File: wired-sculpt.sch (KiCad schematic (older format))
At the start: 26 parts, among them J1 10103594-0001LF, J3 AVR-ISP-6 - NOT FITTED, J4 3-84952-0, SW1 FSMSM, U1 AT90USB1286-AU, U2 USBLC6-2SC6, Y1 TSX-3225 16.0000MF18X-AC6

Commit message: WIP: checkpoint work on rev 3 of the schematic and layout
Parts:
- removed R4, R5, R6: ERJ-3GEYJ331V, Resistor_SMD:R_0603_1608Metric, symbol Device:R_US
- added C10, C11, C12: CL10A105KA8NNNC, Capacitor_SMD:C_0603_1608Metric, symbol Device:C
- added C2: CL21B104KACNNNC, Capacitor_SMD:C_0805_2012Metric, symbol Device:C
- added C3: CL21B103KBANNNC, Capacitor_SMD:C_0805_2012Metric, symbol Device:C
- added Q1: BSS84AK,215, Package_TO_SOT_SMD:SOT-23, symbol Transistor_FET:BSS84
- added Q2: 2N7002, Package_TO_SOT_SMD:SOT-23, symbol Transistor_FET:2N7002
- added R10: ERJ-PA3J473V, Resistor_SMD:R_0603_1608Metric, symbol Device:R_US
- added R11: ERJ-3GEYJ331V, Resistor_SMD:R_0603_1608Metric, symbol Device:R_US
- added R12: ERJ-3EKF10R0V, Resistor_SMD:R_0603_1608Metric, symbol Device:R_US
- added R13: ERJ-PA3J472V, Resistor_SMD:R_0603_1608Metric, symbol Device:R_US
- added R7: ERJ-3EKF8873V, Resistor_SMD:R_0603_1608Metric, symbol Device:R_US
- added SW2: Conn_01x02_Female, Connector_JST:JST_PH_S2B-PH-K_1x02_P2.00mm_Horizontal, symbol Connector:Conn_01x02_Female
- added U3: LM2776, Package_TO_SOT_SMD:SOT-23-6, symbol Regulator_SwitchedCapacitor:LM2776
- C1: value TAJA106K006RNJ -> CL21A475KAQNNNE; footprint Capacitor_Tantalum_SMD:CP_EIA-3216-10_Kemet-I -> Capacitor_SMD:C_0805_2012Metric; symbol Device:CP -> Device:C
- C5, C6, C7: value CL05A104KA5NNNC -> CL10B104KB8NNNC; footprint Capacitor_SMD:C_0402_1005Metric -> Capacitor_SMD:C_0603_1608Metric
- R2: value ERJ-3EKF2200V -> ERJ-3GEYJ331V
- R8: value ERJ-3EKF1001V -> ERJ-3GEYJ103V
- renumbered C2 to C8, C3 to C9
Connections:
- net labels added: -5V, Dout+, Dout-, GREEN+, GREEN-, PB0, RED+
- wire segments 116 -> 146
- no-connect marks 16 -> 15
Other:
- moved on the sheet: C5, C6, C7, C8, C9, D1, R1, R2, R3, R9, SW1, U2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

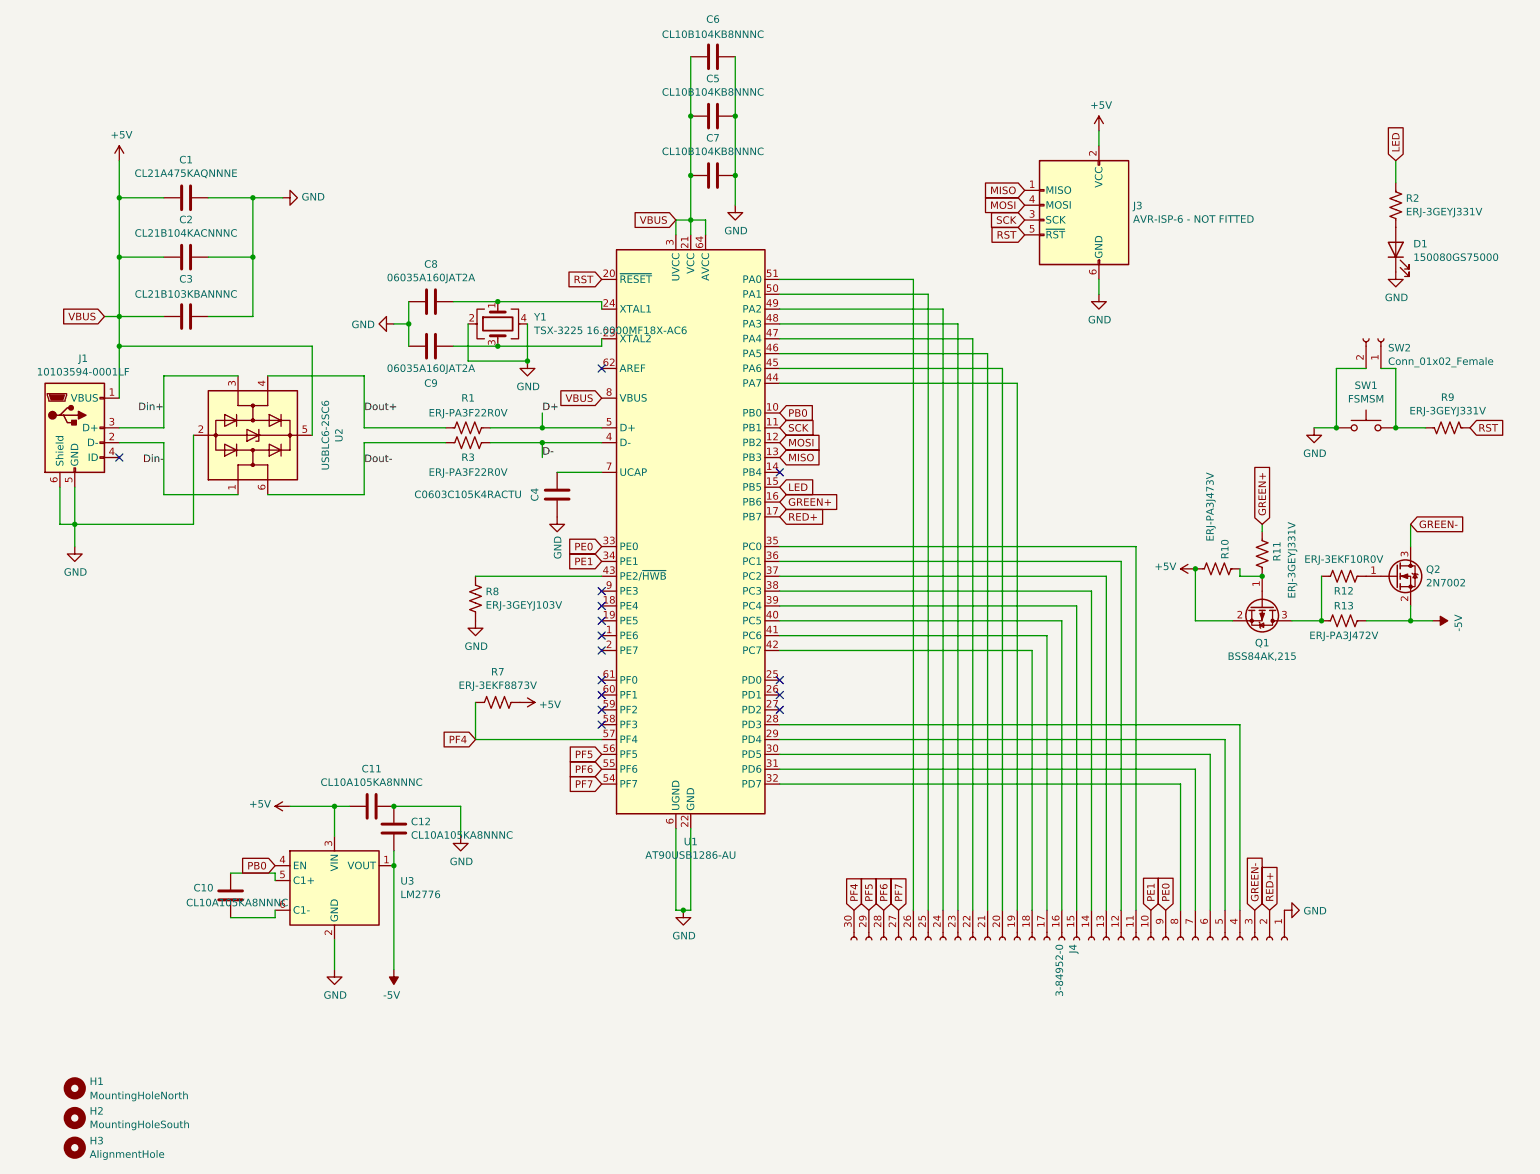
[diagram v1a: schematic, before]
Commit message: renumber the references
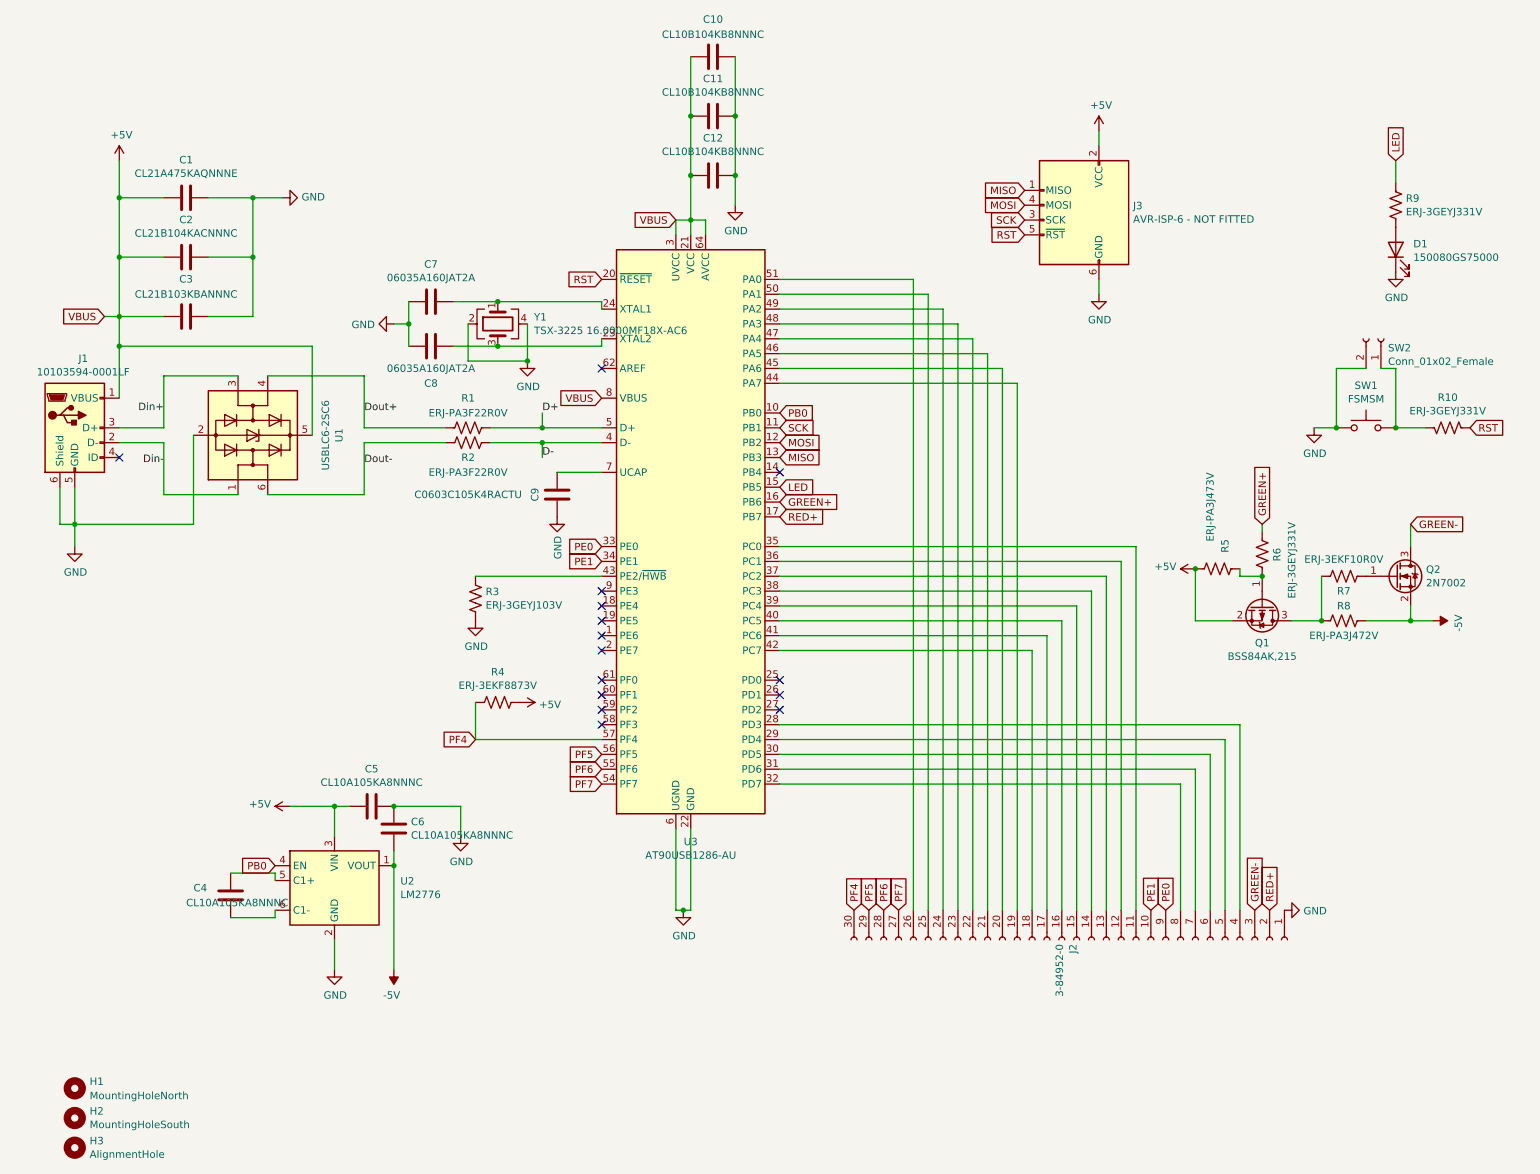
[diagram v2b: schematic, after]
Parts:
- renumbered C6 to C10, C5 to C11, C7 to C12, C10 to C4, C11 to C5, C12 to C6, C8 to C7, C9 to C8, C4 to C9, J4 to J2, R9 to R10, R3 to R2, R8 to R3, R7 to R4, R10 to R5, R11 to R6, R12 to R7, R13 to R8, R2 to R9, U2 to U1, U3 to U2, U1 to U3

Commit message: Move a trace and generate gerbers for Apr 18
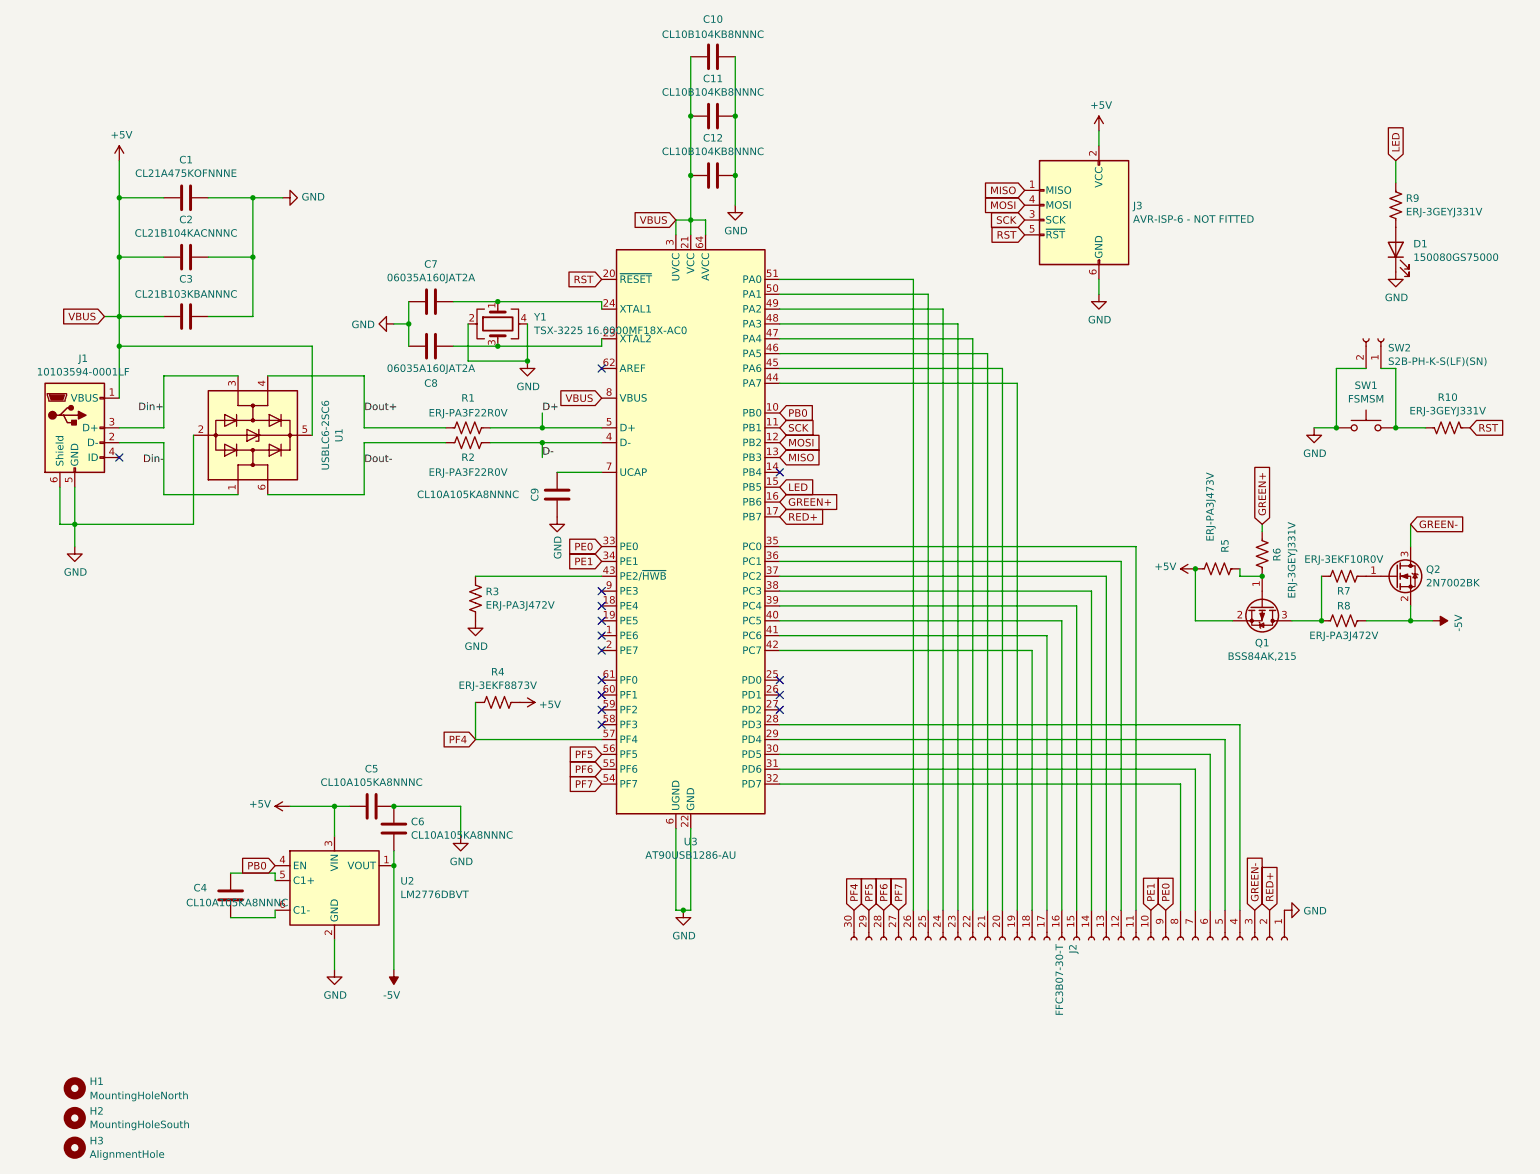
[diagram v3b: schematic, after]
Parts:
- C1: value CL21A475KAQNNNE -> CL21A475KOFNNNE
- C9: value C0603C105K4RACTU -> CL10A105KA8NNNC
- J2: value 3-84952-0 -> FFC3B07-30-T
- Q2: value 2N7002 -> 2N7002BK
- R3: value ERJ-3GEYJ103V -> ERJ-PA3J472V
- SW2: value Conn_01x02_Female -> S2B-PH-K-S(LF)(SN)
- U2: value LM2776 -> LM2776DBVT
- Y1: value TSX-3225 16.0000MF18X-AC6 -> TSX-3225 16.0000MF18X-AC0
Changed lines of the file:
@@
 P 4650 3150
 F 0 "C9" V 4500 3150 50  0000 C CNN
-F 1 "C0603C105K4RACTU" H 4050 3150 50  0000 C CNN
+F 1 "CL10A105KA8NNNC" H 4050 3150 50  0000 C CNN
 F 2 "Capacitor_SMD:C_0603_1608Metric" H 4688 3000 50  0001 C CNN
 F 3 "~" H 4650 3150 50  0001 C CNN
@@
 P 2150 1150
 F 0 "C1" V 1895 1150 50  0000 C CNN
-F 1 "CL21A475KAQNNNE" V 1986 1150 50  0000 C CNN
+F 1 "CL21A475KOFNNNE" V 1986 1150 50  0000 C CNN
 F 2 "Capacitor_SMD:C_0805_2012Metric" H 2188 1000 50  0001 C CNN
 F 3 "~" H 2150 1150 50  0001 C CNN
@@
 P 4250 2000
 F 0 "Y1" V 4204 1756 50  0000 R CNN
-F 1 "TSX-3225 16.0000MF18X-AC6" V 4295 1756 50  0000 R CNN
+F 1 "TSX-3225 16.0000MF18X-AC0" V 4295 1756 50  0000 R CNN
 F 2 "Crystal:Crystal_SMD_3225-4Pin_3.2x2.5mm" H 4250 2000 50  0001 C CNN
-F 3 "~" H 4250 2000 50  0001 C CNN
+F 3 "https://www5.epsondevice.com/en/information/support/pdf/june_2018_psc_masterbook.pdf" H 4250 2000 50  0001 C CNN
 	1    4250 2000
 	0    -1   1    0
@@
 P 4100 3850
 F 0 "R3" H 4168 3896 50  0000 L CNN
-F 1 "ERJ-3GEYJ103V" H 4168 3805 50  0000 L CNN
+F 1 "ERJ-PA3J472V" H 4168 3805 50  0000 L CNN
 F 2 "Resistor_SMD:R_0603_1608Metric" V 4140 3840 50  0001 C CNN
-F 3 "https://industrial.panasonic.com/cdbs/www-data/pdf/RDA0000/AOA0000C304.pdf" H 4100 3850 50  0001 C CNN
+F 3 "" H 4100 3850 50  0001 C CNN
 	1    4100 3850
 	1    0    0    -1
@@
 P 8150 6150
 F 0 "J2" H 8178 6126 50  0000 L CNN
-F 1 "3-84952-0" H 8178 6035 50  0000 L CNN
+F 1 "FFC3B07-30-T" H 8178 6035 50  0000 L CNN
 F 2 "Connector_FFC-FPC:TE_3-84952-0_1x30-1MP_P1.0mm_Horizontal" H 8150 6150 50  0001 C CNN
-F 3 "https://www.te.com/commerce/DocumentDelivery/DDEController?Action=srchrtrv&DocNm=84952&DocType=Customer+Drawing&DocLang=English" H 8150 6150 50  0001 C CNN
+F 3 "https://gct.co/files/specs/1.0mm-ffc-spec.pdf" H 8150 6150 50  0001 C CNN
 	1    8150 6150
 	0    1    1    0
@@
 P 10200 2100
 F 0 "SW2" V 10138 2148 50  0000 L CNN
-F 1 "Conn_01x02_Female" V 10047 2148 50  0000 L CNN
+F 1 "S2B-PH-K-S(LF)(SN)" V 10047 2148 50  0000 L CNN
 F 2 "Connector_JST:JST_PH_S2B-PH-K_1x02_P2.00mm_Horizontal" H 10200 2100 50  0001 C CNN
 F 3 "https://www.jst-mfg.com/product/pdf/eng/ePH.pdf" H 10200 2100 50  0001 C CNN
@@
 P 3150 5750
 F 0 "U2" H 3594 5746 50  0000 L CNN
-F 1 "LM2776" H 3594 5655 50  0000 L CNN
+F 1 "LM2776DBVT" H 3594 5655 50  0000 L CNN
 F 2 "Package_TO_SOT_SMD:SOT-23-6" H 3200 5400 50  0001 L CNN
 F 3 "http://www.ti.com/lit/ds/symlink/lm2776.pdf" H 1300 7000 50  0001 C CNN
@@
 P 10300 3700
 F 0 "Q2" H 10504 3746 50  0000 L CNN
-F 1 "2N7002" H 10504 3655 50  0000 L CNN
+F 1 "2N7002BK" H 10504 3655 50  0000 L CNN
 F 2 "Package_TO_SOT_SMD:SOT-23" H 10500 3625 50  0001 L CIN
-F 3 "https://www.onsemi.com/pub/Collateral/NDS7002A-D.PDF" H 10300 3700 50  0001 L CNN
+F 3 "https://assets.nexperia.com/documents/data-sheet/2N7002BK.pdf" H 10300 3700 50  0001 L CNN
 	1    10300 3700
 	1    0    0    -1
@@
 F 1 "BSS84AK,215" V 9740 3900 50  0000 C CNN
 F 2 "Package_TO_SOT_SMD:SOT-23" H 9600 3825 50  0001 L CIN
-F 3 "http://assets.nexperia.com/documents/data-sheet/BSS84.pdf" H 9400 3900 50  0001 L CNN
+F 3 "https://assets.nexperia.com/documents/data-sheet/BSS84AK.pdf" H 9400 3900 50  0001 L CNN
 	1    9400 3900
 	0    1    1    0

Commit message: fit the schematic on US Letter paper instead of A4
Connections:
- net +5V: now also C10.1, C11.1, C12.1; no longer C10.2, C11.2, C12.2
- net GND: now also C10.2, C11.2, C12.2; no longer C10.1, C11.1, C12.1
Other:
- moved on the sheet: C10, C11, C12, C4, C5, C6, D1, H1, H2, H3, J3, Q1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
